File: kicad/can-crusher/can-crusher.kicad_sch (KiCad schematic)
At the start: 21 parts, among them J1 Stepper Right, J2 Control UART, J3 Ext power, J4 Stepper Left, J5 Barrel_Jack, J6 Expansion Port, Q1 IRF4905, Q2 BS170, SW1 Reboot, SW2 User Interaction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

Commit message: Make board more compact; make power traces appropriate sized.
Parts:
- J2: footprint Connector_PinHeader_2.54mm:PinHeader_1x06_P2.54mm_Vertical -> Connector_PinSocket_2.54mm:PinSocket_1x06_P2.54mm_Vertical
- J6: footprint Connector_PinHeader_2.54mm:PinHeader_1x08_P2.54mm_Vertical -> Connector_PinSocket_2.54mm:PinSocket_1x08_P2.54mm_Vertical
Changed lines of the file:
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@@
     (property "Reference" "J2" (id 0) (at 47.625 15.24 0))
     (property "Value" "Control UART" (id 1) (at 47.625 17.78 0))
-    (property "Footprint" "Connector_PinHeader_2.54mm:PinHeader_1x06_P2.54mm_Vertical" (id 2) (at 46.99 25.4 0)
+    (property "Footprint" "Connector_PinSocket_2.54mm:PinSocket_1x06_P2.54mm_Vertical" (id 2) (at 46.99 25.4 0)
       (effects (font (size 1.27 1.27)) hide)
     )
@@
     (property "Reference" "J6" (id 0) (at 143.51 26.67 90))
     (property "Value" "Expansion Port" (id 1) (at 143.51 29.21 90))
-    (property "Footprint" "Connector_PinHeader_2.54mm:PinHeader_1x08_P2.54mm_Vertical" (id 2) (at 142.24 31.75 0)
+    (property "Footprint" "Connector_PinSocket_2.54mm:PinSocket_1x08_P2.54mm_Vertical" (id 2) (at 142.24 31.75 0)
       (effects (font (size 1.27 1.27)) hide)
     )
@@
     )
     (path "/352d29cf-338d-4da2-ac95-5b42ce304865"
-      (reference "J2") (unit 1) (value "Control UART") (footprint "Connector_PinHeader_2.54mm:PinHeader_1x06_P2.54mm_Vertical")
+      (reference "J2") (unit 1) (value "Control UART") (footprint "Connector_PinSocket_2.54mm:PinSocket_1x06_P2.54mm_Vertical")
     )
     (path "/467346d6-c529-4c94-bbb6-f1fa2d06a5d2"
@@
     )
     (path "/ee2482f5-d6df-4154-b36c-d36bee7d0ea9"
-      (reference "J6") (unit 1) (value "Expansion Port") (footprint "Connector_PinHeader_2.54mm:PinHeader_1x08_P2.54mm_Vertical")
+      (reference "J6") (unit 1) (value "Expansion Port") (footprint "Connector_PinSocket_2.54mm:PinSocket_1x08_P2.54mm_Vertical")
     )
     (path "/e9821278-bb88-4a3b-a615-62bf01f96eed"

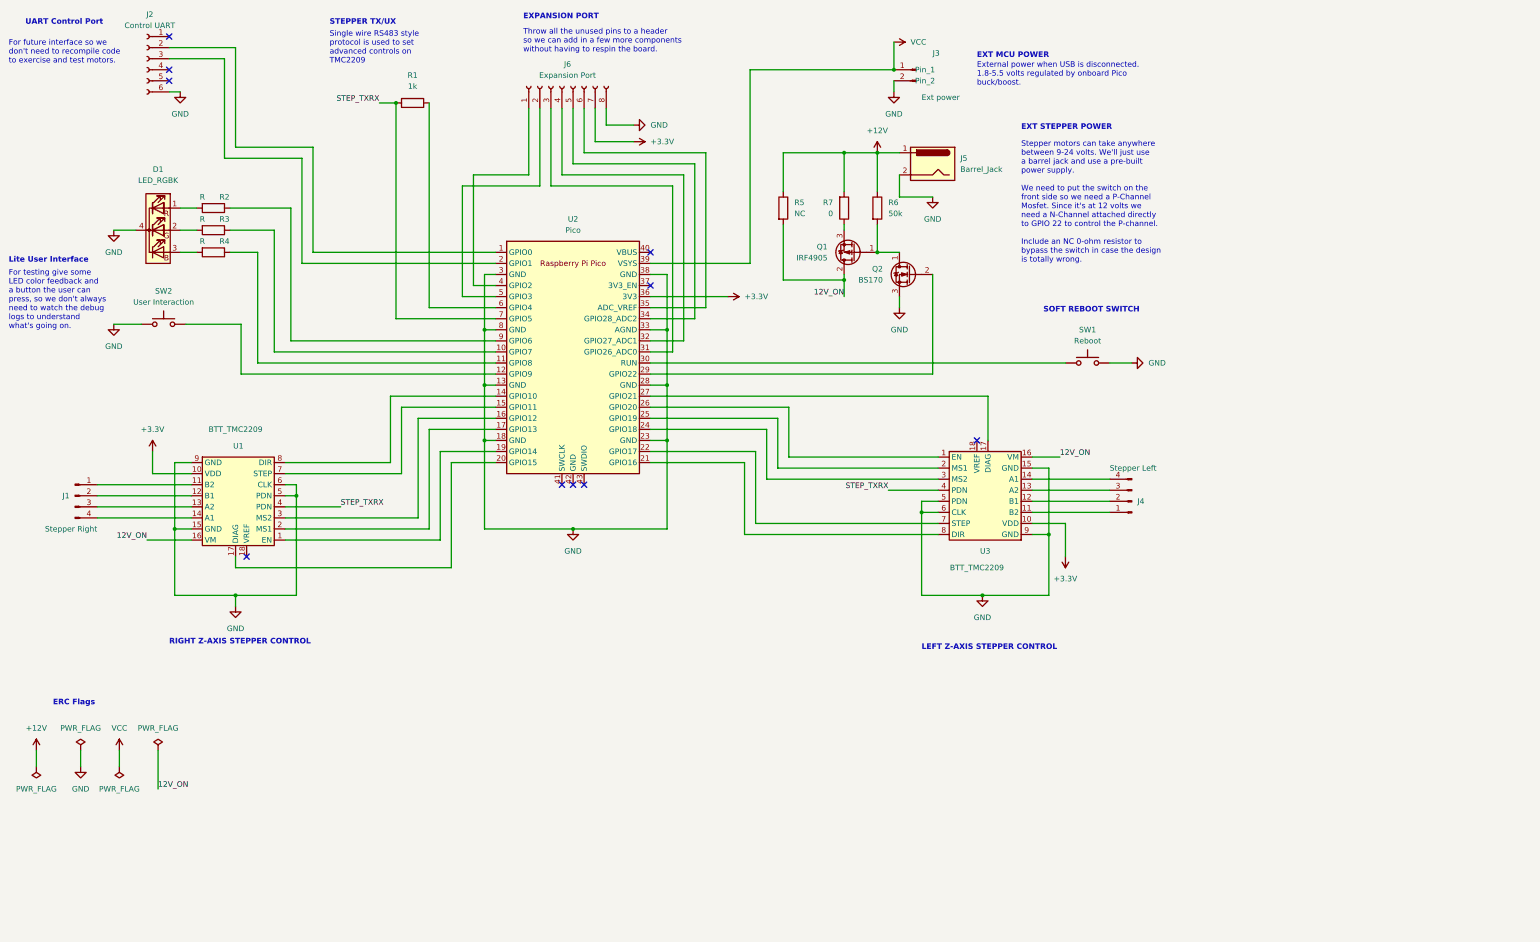
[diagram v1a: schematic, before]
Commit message: Final REV 1 control board submitted for PCB manufacturing
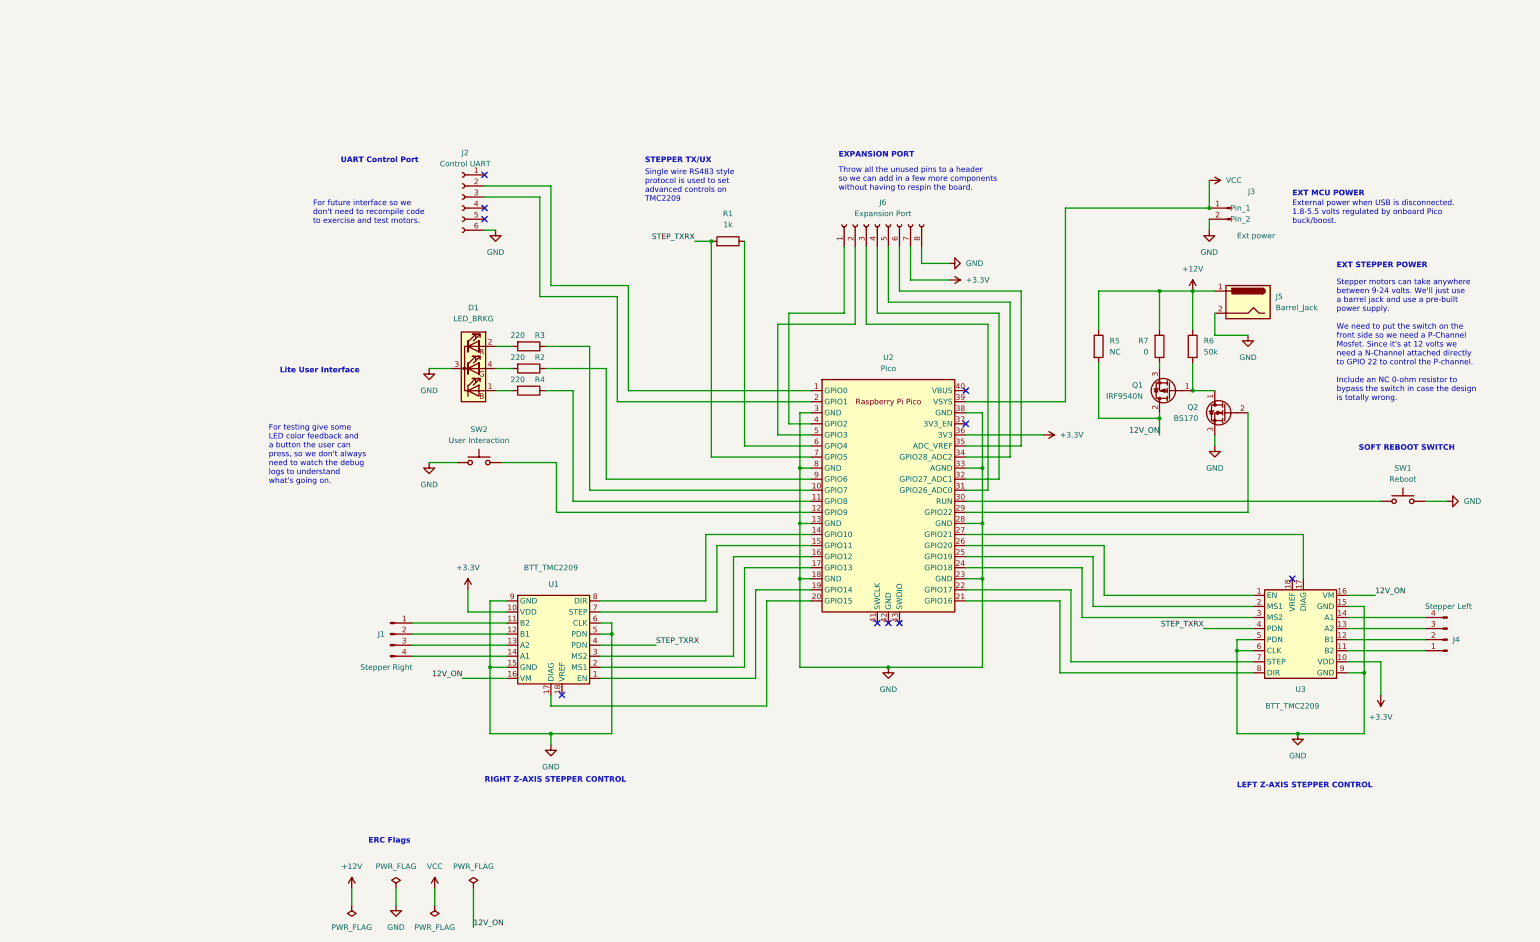
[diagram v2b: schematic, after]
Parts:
- D1: value LED_RGBK -> LED_BRKG; symbol Device:LED_RGBK -> Device:LED_BRKG
- Q1: value IRF4905 -> IRF9540N; symbol Transistor_FET:IRF4905 -> Transistor_FET:IRF9540N
- R2, R3, R4: value R -> 220
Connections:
- net GND: now also D1.3 (K); no longer D1.4 (K)
- net at R2.2: now also D1.4 (GA); no longer D1.1 (RA)
- net at R4.2: now also D1.1 (BA); no longer D1.3 (BA)
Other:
- moved on the sheet: D1, J1, J2, J3, J4, J5, J6, Q1, Q2, R1, R2, R3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

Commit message: Add pull down to power circuitry
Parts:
- added R8: 57.6k, Resistor_THT:R_Axial_DIN0207_L6.3mm_D2.5mm_P10.16mm_Horizontal, symbol Device:R
- R6: value 50k -> 57.6k
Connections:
- net GND: now also R8.2
- net at Q2.2 (G), U2.29 (GPIO22): now also R8.1
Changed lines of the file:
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@@
   (junction (at 326.39 166.37) (diameter 0) (color 0 0 0 0)
+  )
+  (junction (at 299.72 106.68) (diameter 0) (color 0 0 0 0)
   )
   (junction (at 196.85 144.78) (diameter 0) (color 0 0 0 0)
@@
     (stroke (width 0) (type default) (color 0 0 0 0))
   )
+  (wire (pts (xy 311.15 106.68) (xy 314.96 106.68))
+    (stroke (width 0) (type default) (color 0 0 0 0))
+  )
   (wire (pts (xy 121.92 215.9) (xy 121.92 224.79))
     (stroke (width 0) (type default) (color 0 0 0 0))
@@
   )
   (wire (pts (xy 175.26 134.62) (xy 175.26 149.86))
+    (stroke (width 0) (type default) (color 0 0 0 0))
+  )
+  (wire (pts (xy 299.72 106.68) (xy 303.53 106.68))
     (stroke (width 0) (type default) (color 0 0 0 0))
   )
@@
       (effects (font (size 1.27 1.27)) (justify left))
     )
-    (property "Value" "50k" (id 1) (at 289.56 92.7099 0)
+    (property "Value" "57.6k" (id 1) (at 289.56 92.7099 0)
       (effects (font (size 1.27 1.27)) (justify left))
     )
@@
     (pin "1")
   )
+  (symbol (lib_id "power:GND") (at 314.96 106.68 0) (unit 1)
+    (in_bom yes) (on_board yes) (fields_autoplaced)
+    (property "Reference" "#PWR0105" (id 0) (at 314.96 113.03 0)
+      (effects (font (size 1.27 1.27)) hide)
+    )
+    (property "Value" "GND" (id 1) (at 314.96 111.76 0))
+    (property "Footprint" "" (id 2) (at 314.96 106.68 0)
+      (effects (font (size 1.27 1.27)) hide)
+    )
+    (property "Datasheet" "" (id 3) (at 314.96 106.68 0)
+      (effects (font (size 1.27 1.27)) hide)
+    )
+    (pin "1")
+  )
   (symbol (lib_id "power:+3.3V") (at 330.2 171.45 0) (mirror x) (unit 1)
     (in_bom yes) (on_board yes) (fields_autoplaced)
@@
     )
     (pin "1")
+  )
+  (symbol (lib_id "Device:R") (at 307.34 106.68 90) (unit 1)
+    (in_bom yes) (on_board yes) (fields_autoplaced)
+    (property "Reference" "R8" (id 0) (at 307.34 100.33 90))
+    (property "Value" "57.6k" (id 1) (at 307.34 102.87 90))
+    (property "Footprint" "Resistor_THT:R_Axial_DIN0207_L6.3mm_D2.5mm_P10.16mm_Horizontal" (id 2) (at 307.34 108.458 90)
+      (effects (font (size 1.27 1.27)) hide)
+    )
+    (property "Datasheet" "~" (id 3) (at 307.34 106.68 0)
+      (effects (font (size 1.27 1.27)) hide)
+    )
+    (pin "1")
+    (pin "2")
   )
   (symbol (lib_id "Transistor_FET:IRF9540N") (at 281.94 101.6 180) (unit 1)
@@
       (reference "#PWR0104") (unit 1) (value "GND") (footprint "")
     )
+    (path "/befac66d-a5da-4899-ad84-177af15b88e2"
+      (reference "#PWR0105") (unit 1) (value "GND") (footprint "")
+    )
     (path "/844af557-77cd-4209-bc80-ef3cd86ed783"
       (reference "D1") (unit 1) (value "LED_BRKG") (footprint "LED_THT:LED_D5.0mm-4_RGB")
@@
     )
     (path "/66b0f66d-ec9b-4513-957e-aad8729e8b47"
-      (reference "R6") (unit 1) (value "50k") (footprint "Resistor_THT:R_Axial_DIN0207_L6.3mm_D2.5mm_P10.16mm_Horizontal")
+      (reference "R6") (unit 1) (value "57.6k") (footprint "Resistor_THT:R_Axial_DIN0207_L6.3mm_D2.5mm_P10.16mm_Horizontal")
     )
     (path "/d5851b35-de6c-4a0d-9963-b0e63428b0ab"
       (reference "R7") (unit 1) (value "0") (footprint "Resistor_THT:R_Axial_DIN0207_L6.3mm_D2.5mm_P10.16mm_Horizontal")
     )
+    (path "/e89ff249-05a6-4819-a964-b52cc99a4621"
+      (reference "R8") (unit 1) (value "57.6k") (footprint "Resistor_THT:R_Axial_DIN0207_L6.3mm_D2.5mm_P10.16mm_Horizontal")
+    )
     (path "/d7f64b4f-4359-41c8-a3c5-9e6bef533109"

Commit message: Start moving to SMD components
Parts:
- Q2: value BS170 -> MMBF170; footprint Package_TO_SOT_THT:TO-92_Inline -> Package_TO_SOT_SMD:SOT-23; symbol Transistor_FET:BS170 -> Transistor_FET:MMBF170
- R1, R2, R3, R4, R8: footprint Resistor_THT:R_Axial_DIN0207_L6.3mm_D2.5mm_P10.16mm_Horizontal -> Resistor_SMD:R_0805_2012Metric
- R5, R6, R7: footprint Resistor_THT:R_Axial_DIN0207_L6.3mm_D2.5mm_P10.16mm_Horizontal -> Resistor_SMD:R_1206_3216Metric
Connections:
- net GND: now also Q2.2 (S); no longer Q2.3 (S)
- net at Q1.1 (G), R6.2: now also Q2.3 (D); no longer Q2.1 (D)
- net at R8.1, U2.29 (GPIO22): now also Q2.1 (G); no longer Q2.2 (G)
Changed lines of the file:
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@@
       (effects (font (size 1.27 1.27)) (justify left))
     )
-    (property "Footprint" "Resistor_THT:R_Axial_DIN0207_L6.3mm_D2.5mm_P10.16mm_Horizontal" (id 2) (at 263.652 91.44 90)
+    (property "Footprint" "Resistor_SMD:R_1206_3216Metric" (id 2) (at 263.652 91.44 90)
       (effects (font (size 1.27 1.27)) hide)
     )
@@
     (property "Reference" "R3" (id 0) (at 137.16 88.9 90))
     (property "Value" "220" (id 1) (at 132.08 88.9 90))
-    (property "Footprint" "Resistor_THT:R_Axial_DIN0207_L6.3mm_D2.5mm_P10.16mm_Horizontal" (id 2) (at 134.62 89.662 90)
+    (property "Footprint" "Resistor_SMD:R_0805_2012Metric" (id 2) (at 134.62 89.662 90)
       (effects (font (size 1.27 1.27)) hide)
     )
@@
     (pin "1")
   )
-  (symbol (lib_id "Transistor_FET:BS170") (at 294.64 106.68 0) (mirror y) (unit 1)
+  (symbol (lib_id "Transistor_FET:MMBF170") (at 294.64 106.68 0) (mirror y) (unit 1)
     (in_bom yes) (on_board yes) (fields_autoplaced)
     (property "Reference" "Q2" (id 0) (at 288.29 105.4099 0)
       (effects (font (size 1.27 1.27)) (justify left))
     )
-    (property "Value" "BS170" (id 1) (at 288.29 107.9499 0)
-      (effects (font (size 1.27 1.27)) (justify left))
-    )
-    (property "Footprint" "Package_TO_SOT_THT:TO-92_Inline" (id 2) (at 289.56 108.585 0)
+    (property "Value" "MMBF170" (id 1) (at 288.29 107.9499 0)
+      (effects (font (size 1.27 1.27)) (justify left))
+    )
+    (property "Footprint" "Package_TO_SOT_SMD:SOT-23" (id 2) (at 289.56 108.585 0)
       (effects (font (size 1.27 1.27) italic) (justify left) hide)
     )
-    (property "Datasheet" "https://www.onsemi.com/pub/Collateral/BS170-D.PDF" (id 3) (at 294.64 106.68 0)
+    (property "Datasheet" "https://www.diodes.com/assets/Datasheets/ds30104.pdf" (id 3) (at 294.64 106.68 0)
       (effects (font (size 1.27 1.27)) (justify left) hide)
     )
@@
     (property "Reference" "R2" (id 0) (at 137.16 93.98 90))
     (property "Value" "220" (id 1) (at 132.08 93.98 90))
-    (property "Footprint" "Resistor_THT:R_Axial_DIN0207_L6.3mm_D2.5mm_P10.16mm_Horizontal" (id 2) (at 134.62 94.742 90)
+    (property "Footprint" "Resistor_SMD:R_0805_2012Metric" (id 2) (at 134.62 94.742 90)
       (effects (font (size 1.27 1.27)) hide)
     )
@@
     (property "Reference" "R4" (id 0) (at 137.16 99.06 90))
     (property "Value" "220" (id 1) (at 132.08 99.06 90))
-    (property "Footprint" "Resistor_THT:R_Axial_DIN0207_L6.3mm_D2.5mm_P10.16mm_Horizontal" (id 2) (at 134.62 99.822 90)
+    (property "Footprint" "Resistor_SMD:R_0805_2012Metric" (id 2) (at 134.62 99.822 90)
       (effects (font (size 1.27 1.27)) hide)
     )
@@
       (effects (font (size 1.27 1.27)) (justify left))
     )
-    (property "Footprint" "Resistor_THT:R_Axial_DIN0207_L6.3mm_D2.5mm_P10.16mm_Horizontal" (id 2) (at 285.242 91.44 90)
+    (property "Footprint" "Resistor_SMD:R_1206_3216Metric" (id 2) (at 285.242 91.44 90)
       (effects (font (size 1.27 1.27)) hide)
     )
@@
     (property "Reference" "R1" (id 0) (at 180.34 60.96 90))
     (property "Value" "1k" (id 1) (at 180.34 63.5 90))
-    (property "Footprint" "Resistor_THT:R_Axial_DIN0207_L6.3mm_D2.5mm_P10.16mm_Horizontal" (id 2) (at 180.34 69.088 90)
+    (property "Footprint" "Resistor_SMD:R_0805_2012Metric" (id 2) (at 180.34 69.088 90)
       (effects (font (size 1.27 1.27)) hide)
     )
@@
       (effects (font (size 1.27 1.27)) (justify right))
     )
-    (property "Footprint" "Resistor_THT:R_Axial_DIN0207_L6.3mm_D2.5mm_P10.16mm_Horizontal" (id 2) (at 277.622 91.44 90)
+    (property "Footprint" "Resistor_SMD:R_1206_3216Metric" (id 2) (at 277.622 91.44 90)
       (effects (font (size 1.27 1.27)) hide)
     )
@@
     (property "Reference" "R8" (id 0) (at 307.34 100.33 90))
     (property "Value" "57.6k" (id 1) (at 307.34 102.87 90))
-    (property "Footprint" "Resistor_THT:R_Axial_DIN0207_L6.3mm_D2.5mm_P10.16mm_Horizontal" (id 2) (at 307.34 108.458 90)
+    (property "Footprint" "Resistor_SMD:R_0805_2012Metric" (id 2) (at 307.34 108.458 90)
       (effects (font (size 1.27 1.27)) hide)
     )
@@
     )
     (path "/2bc33def-5d0c-4e21-9108-450ffb8a11e8"
-      (reference "Q2") (unit 1) (value "BS170") (footprint "Package_TO_SOT_THT:TO-92_Inline")
+      (reference "Q2") (unit 1) (value "MMBF170") (footprint "Package_TO_SOT_SMD:SOT-23")
     )
     (path "/89ba5f73-6abc-4cac-905d-5cb868e67519"
-      (reference "R1") (unit 1) (value "1k") (footprint "Resistor_THT:R_Axial_DIN0207_L6.3mm_D2.5mm_P10.16mm_Horizontal")
+      (reference "R1") (unit 1) (value "1k") (footprint "Resistor_SMD:R_0805_2012Metric")
     )
     (path "/388daa19-32b8-4822-931e-899ce41b3f8e"
-      (reference "R2") (unit 1) (value "220") (footprint "Resistor_THT:R_Axial_DIN0207_L6.3mm_D2.5mm_P10.16mm_Horizontal")
+      (reference "R2") (unit 1) (value "220") (footprint "Resistor_SMD:R_0805_2012Metric")
     )
     (path "/24a1b262-7634-421a-8b74-f27e23e7b847"
-      (reference "R3") (unit 1) (value "220") (footprint "Resistor_THT:R_Axial_DIN0207_L6.3mm_D2.5mm_P10.16mm_Horizontal")
+      (reference "R3") (unit 1) (value "220") (footprint "Resistor_SMD:R_0805_2012Metric")
     )
     (path "/40c4e155-e1fd-4340-ba77-29e9a89c9ee1"
-      (reference "R4") (unit 1) (value "220") (footprint "Resistor_THT:R_Axial_DIN0207_L6.3mm_D2.5mm_P10.16mm_Horizontal")
+      (reference "R4") (unit 1) (value "220") (footprint "Resistor_SMD:R_0805_2012Metric")
     )
     (path "/1f199d61-f9c4-429a-9371-ca91503c663f"
-      (reference "R5") (unit 1) (value "NC") (footprint "Resistor_THT:R_Axial_DIN0207_L6.3mm_D2.5mm_P10.16mm_Horizontal")
+      (reference "R5") (unit 1) (value "NC") (footprint "Resistor_SMD:R_1206_3216Metric")
     )
     (path "/66b0f66d-ec9b-4513-957e-aad8729e8b47"
-      (reference "R6") (unit 1) (value "57.6k") (footprint "Resistor_THT:R_Axial_DIN0207_L6.3mm_D2.5mm_P10.16mm_Horizontal")
+      (reference "R6") (unit 1) (value "57.6k") (footprint "Resistor_SMD:R_1206_3216Metric")
     )
     (path "/d5851b35-de6c-4a0d-9963-b0e63428b0ab"
-      (reference "R7") (unit 1) (value "0") (footprint "Resistor_THT:R_Axial_DIN0207_L6.3mm_D2.5mm_P10.16mm_Horizontal")
+      (reference "R7") (unit 1) (value "0") (footprint "Resistor_SMD:R_1206_3216Metric")
     )
     (path "/e89ff249-05a6-4819-a964-b52cc99a4621"
-      (reference "R8") (unit 1) (value "57.6k") (footprint "Resistor_THT:R_Axial_DIN0207_L6.3mm_D2.5mm_P10.16mm_Horizontal")
+      (reference "R8") (unit 1) (value "57.6k") (footprint "Resistor_SMD:R_0805_2012Metric")
     )
     (path "/d7f64b4f-4359-41c8-a3c5-9e6bef533109"
